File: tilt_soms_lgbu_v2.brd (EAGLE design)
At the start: 36 x 130 mm, 37 parts

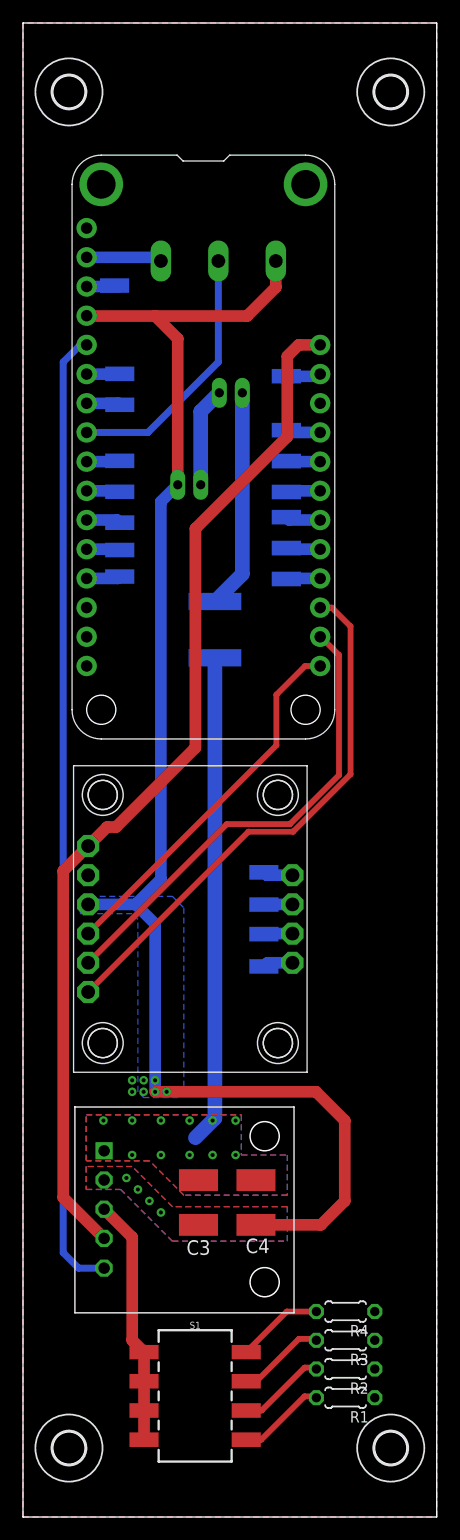
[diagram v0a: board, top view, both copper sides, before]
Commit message: Added a v2 for the tilt_soms_lgbu board (tilt_soms_lgbu_v2)
Primary changes:
Placed all components on top layer including the con-wago connectors.
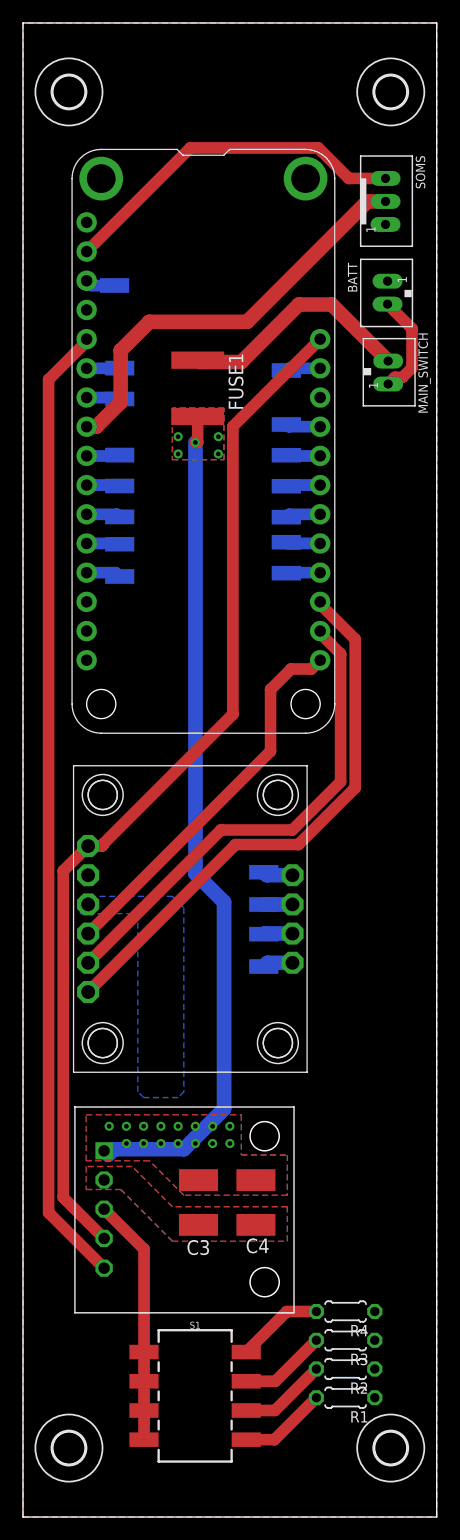
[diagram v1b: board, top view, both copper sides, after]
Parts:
- SOMS: value (none) -> JST-PH_3-PIN_HEADER; device con-wago-500:W237-103 -> SRG:JST_B3B-PH_HEADER
- moved BATT 24.0 mm to (31.8, 106.5), flipped to the top, turned to 90 degrees
- moved FUSE1 21.1 mm to (15.2, 98.2), flipped to the top
- moved SOMS 15.9 mm to (31.5, 114.5), flipped to the top, turned to 270 degrees
- moved MAIN_SWITCH 13.7 mm to (31.7, 99.7), flipped to the top, turned to 270 degrees
- moved MS1 0.50 mm to (4.27, 119.0)
- moved PAD20 0.50 mm to (8.42, 100.0)
- moved PAD21 0.50 mm to (8.42, 97.3)
- moved PAD23 0.50 mm to (8.42, 92.4)
- moved PAD24 0.50 mm to (8.42, 89.7)
- moved PAD25 0.50 mm to (8.42, 87.0)
- moved PAD27 0.50 mm to (8.42, 84.6)
- moved PAD29 0.50 mm to (22.9, 99.8)
- moved PAD30 0.50 mm to (22.9, 95.1)
- moved PAD31 0.50 mm to (22.9, 92.4)
- moved PAD32 0.50 mm to (22.9, 89.7)
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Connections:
- net FEATHER_3.3V: now also SOMS.P3; no longer SOMS.1
- net GND: now also SOMS.P1; no longer SOMS.3
- net GPIOA3: now also SOMS.P2; no longer SOMS.2
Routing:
- net GND: track 127.6 -> 0.00 mm, vias 11 -> 0
- net VOLTAGE_SUPPLY: track 42.5 -> 73.7 mm, vias 11 -> 20
- net FEATHER_3.3V: track 6.59 -> 30.8 mm
- net GPIOA3: track 22.8 -> 36.8 mm
- net N$4: track 19.1 -> 20.8 mm
- net GPIO5: track 46.9 -> 48.0 mm
- net RPI_SCL: track 41.3 -> 42.3 mm
- net RPI_SDA: track 32.4 -> 33.2 mm
- net AREF: track 3.28 -> 2.60 mm

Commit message: Reversed board. Snap to mills grid.
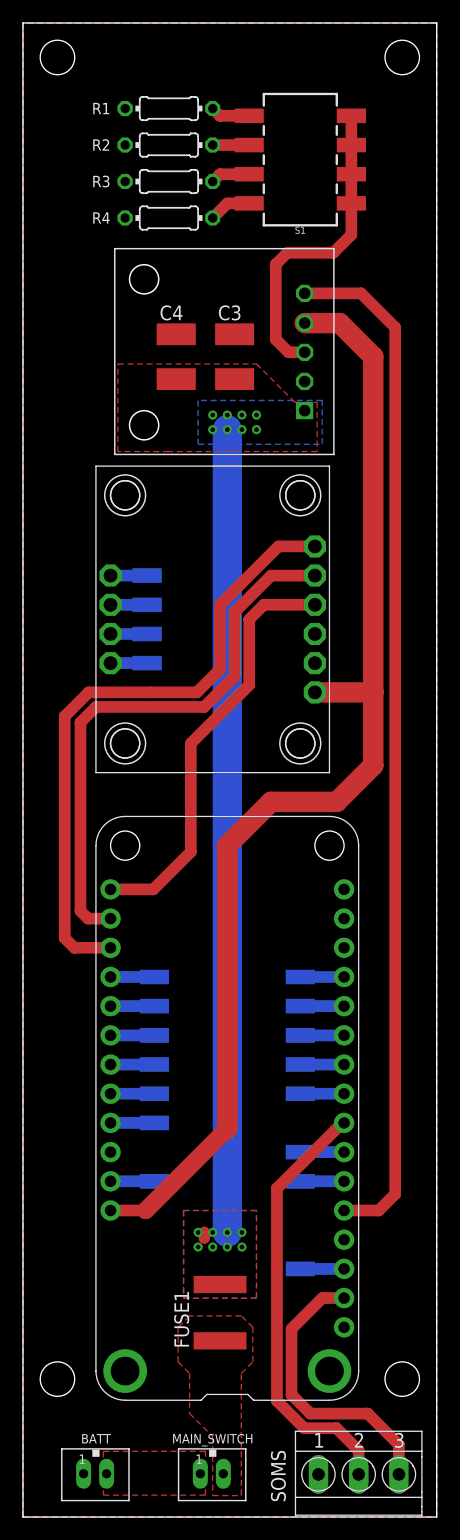
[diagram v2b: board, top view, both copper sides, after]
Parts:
- removed H5, H6, H7, H8: MOUNT-HOLE2.8, holes:2,8
- R1, R2, R3, R4: device rcl:0204/5 -> rcl:0204/7
- SOMS: value JST-PH_3-PIN_HEADER -> TERMINAL-BLOCK-3.5MM-3-PIN-LONG-PAD; device SRG:JST_B3B-PH_HEADER -> Rembrandt Electronics - Terminal Block 3-5mm v1-0:TERMINAL-BLOCK-3-PIN-3.5MM-LONG-PAD
- moved R1 113.2 mm to (12.7, 122.6), turned to 0 degrees
- moved MS1 111.7 mm to (29.2, 10.2), turned to 90 degrees
- moved SOMS 110.7 mm to (29.2, 3.81), turned to 0 degrees
- moved S1 108.0 mm to (24.1, 118.1), turned to 90 degrees
- moved R2 107.6 mm to (12.7, 119.4), turned to 0 degrees
- moved BATT 105.8 mm to (6.35, 3.81), turned to 180 degrees
- moved R3 102.0 mm to (12.7, 116.2), turned to 0 degrees
- moved MAIN_SWITCH 97.1 mm to (16.5, 3.81), turned to 180 degrees
- moved R4 96.4 mm to (12.7, 113.0), turned to 0 degrees
- moved PAD13 87.1 mm to (24.1, 21.6), turned to 270 degrees
- moved FUSE1 80.5 mm to (17.1, 17.8), turned to 90 degrees
- moved C4 73.9 mm to (13.3, 101.0), turned to 90 degrees
- moved C3 73.7 mm to (18.4, 101.0), turned to 90 degrees
- moved PAD20 72.5 mm to (24.1, 29.2), turned to 90 degrees
- moved PAD29 71.5 mm to (11.4, 29.2), turned to 90 degrees
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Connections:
- net FEATHER_3.3V: now also SOMS.3; no longer SOMS.P3
- net GND: now also SOMS.1; no longer SOMS.P1
- net GPIOA3: now also SOMS.2; no longer SOMS.P2
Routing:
- net N$4: track 20.8 -> 0.46 mm
- net FEATHER_BAT: track 89.7 -> 101.2 mm
- net N$3: track 9.07 -> 0.00 mm
- net GPIO5: track 48.0 -> 54.8 mm
- net DELAY: track 21.5 -> 27.5 mm
- net RPI_SCL: track 42.3 -> 48.3 mm
- net FEATHER_3.3V: track 30.8 -> 25.1 mm
- net DONE_PIN: track 84.2 -> 89.5 mm
- net N$10: track 7.60 -> 3.17 mm
- net N$9: track 7.62 -> 3.44 mm
- net N$11: track 7.58 -> 3.44 mm
- net N$12: track 7.57 -> 3.70 mm
- net RPI_SDA: track 33.2 -> 36.9 mm
- net VOLTAGE_SUPPLY: track 73.7 -> 70.3 mm, vias 20 -> 16
- net AREF: track 2.60 -> 3.81 mm
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- added copper zone on layer 1, net N$3
- added copper zone on layer 1, net N$4

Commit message: no dip switch
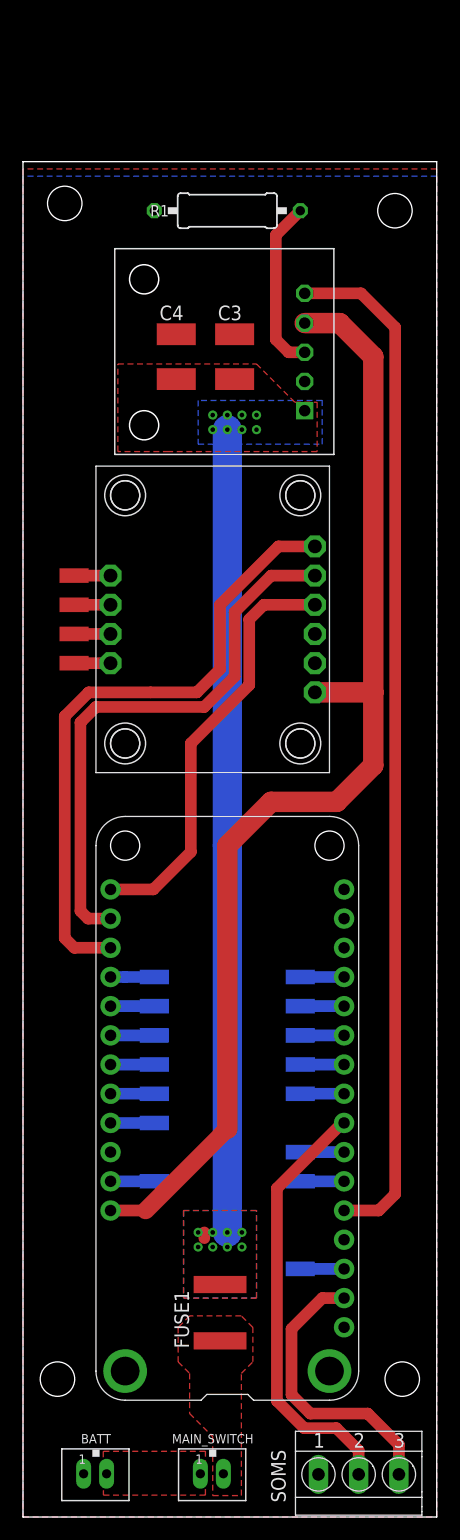
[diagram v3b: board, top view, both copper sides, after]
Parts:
- removed R2, R3, R4: (no value), rcl:0204/7
- removed S1: DIP-04SMD, SparkFun-Switches:DIPSWITCH-04-SMD
- R1: device rcl:0204/7 -> rcl:0309/12
- moved R1 10.2 mm to (17.8, 113.7)
- moved PAD37 6.35 mm to (4.45, 79.4), flipped to the top
- moved PAD38 6.35 mm to (4.45, 81.9), flipped to the top
- moved PAD39 6.35 mm to (4.45, 74.3), flipped to the top
- moved PAD40 6.35 mm to (4.45, 76.8), flipped to the top
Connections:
- removed net N$10: R2.2, S1.3
- removed net N$11: R3.2, S1.2
- removed net N$12: R4.2, S1.1
- removed net N$9: R1.2, S1.4
- net DELAY: now also R1.2; no longer S1.5, S1.6, S1.7, S1.8
- net GND: no longer R2.1, R3.1, R4.1
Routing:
- net DELAY: track 27.5 -> 15.1 mm
- net N$12: track 3.70 -> 0.00 mm
- net N$9: track 3.44 -> 0.00 mm
- net N$11: track 3.44 -> 0.00 mm
- net N$10: track 3.17 -> 0.00 mm
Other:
- board size 36 x 130 mm -> 36 x 117.9 mm
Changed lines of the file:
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@@
 <board>
 <plain>
-<wire x1="36" y1="130" x2="0" y2="130" width="0" layer="20"/>
-<wire x1="0" y1="130" x2="0" y2="0" width="0" layer="20"/>
+<wire x1="36" y1="117.935" x2="0" y2="117.935" width="0" layer="20"/>
+<wire x1="0" y1="117.935" x2="0" y2="0" width="0" layer="20"/>
 <wire x1="0" y1="0" x2="36" y2="0" width="0" layer="20"/>
-<wire x1="36" y1="0" x2="36" y2="130" width="0" layer="20"/>
+<wire x1="36" y1="0" x2="36" y2="117.935" width="0" layer="20"/>
 <dimension x1="0" y1="0" x2="0" y2="130" x3="-17.5" y3="65" textsize="1.778" layer="49"/>
 <dimension x1="0" y1="130" x2="36" y2="130" x3="18" y3="144" textsize="1.778" layer="49"/>
 <hole x="33" y="12" drill="3"/>
 <hole x="3" y="12" drill="3"/>
-<hole x="33" y="127" drill="3"/>
-<hole x="3" y="127" drill="3"/>
+<hole x="32.365" y="113.665" drill="3"/>
+<hole x="3.635" y="114.3" drill="3"/>
 </plain>
 <attributes>
@@
 <element name="PAD34" library="wirepad" package="SMD1,27-2,54" value="WIREPADSMD1,27-254" x="11.43" y="44.45" smashed="yes" rot="MR90"/>
 <element name="PAD35" library="wirepad" package="SMD1,27-2,54" value="WIREPADSMD1,27-254" x="11.43" y="46.99" smashed="yes" rot="MR90"/>
-<element name="PAD37" library="wirepad" package="SMD1,27-2,54" value="WIREPADSMD1,27-254" x="10.795" y="79.375" smashed="yes" rot="MR270"/>
-<element name="PAD38" library="wirepad" package="SMD1,27-2,54" value="WIREPADSMD1,27-254" x="10.795" y="81.915" smashed="yes" rot="MR270"/>
-<element name="PAD39" library="wirepad" package="SMD1,27-2,54" value="WIREPADSMD1,27-254" x="10.795" y="74.295" smashed="yes" rot="MR270"/>
-<element name="PAD40" library="wirepad" package="SMD1,27-2,54" value="WIREPADSMD1,27-254" x="10.795" y="76.835" smashed="yes" rot="MR270"/>
-<element name="R1" library="rcl" package="0204/7" value="" x="12.7" y="122.555" smashed="yes">
-<attribute name="NAME" x="7.62" y="122.555" size="0.9906" layer="25" ratio="10" align="center-right"/>
-<attribute name="VALUE" x="11.0744" y="122.0724" size="0.9906" layer="27" ratio="10"/>
-</element>
-<element name="R2" library="rcl" package="0204/7" value="" x="12.7" y="119.38" smashed="yes">
-<attribute name="NAME" x="7.62" y="119.38" size="0.9906" layer="25" ratio="10" align="center-right"/>
-<attribute name="VALUE" x="11.0744" y="118.8974" size="0.9906" layer="27" ratio="10"/>
-</element>
-<element name="R3" library="rcl" package="0204/7" value="" x="12.7" y="116.205" smashed="yes">
-<attribute name="NAME" x="7.62" y="116.205" size="0.9906" layer="25" ratio="10" align="center-right"/>
-<attribute name="VALUE" x="11.0744" y="115.7224" size="0.9906" layer="27" ratio="10"/>
-</element>
-<element name="R4" library="rcl" package="0204/7" value="" x="12.7" y="113.03" smashed="yes">
-<attribute name="NAME" x="7.62" y="113.03" size="0.9906" layer="25" ratio="10" align="center-right"/>
-<attribute name="VALUE" x="11.0744" y="112.5474" size="0.9906" layer="27" ratio="10"/>
-</element>
-<element name="S1" library="SparkFun-Switches" package="DIPSWITCH-04-SMD" value="DIP-04SMD" x="24.13" y="118.11" smashed="yes" rot="R90">
-<attribute name="NAME" x="24.13" y="112.268" size="0.6096" layer="25" font="vector" ratio="20" rot="R180" align="bottom-center"/>
-<attribute name="PROD_ID" value="SWCH-12418" x="24.13" y="118.11" size="1.778" layer="27" rot="R90" display="off"/>
-<attribute name="VALUE" x="24.13" y="123.952" size="0.6096" layer="27" font="vector" ratio="20" rot="R180" align="top-center"/>
+<element name="PAD37" library="wirepad" package="SMD1,27-2,54" value="WIREPADSMD1,27-254" x="4.445" y="79.375" smashed="yes" rot="R270"/>
+<element name="PAD38" library="wirepad" package="SMD1,27-2,54" value="WIREPADSMD1,27-254" x="4.445" y="81.915" smashed="yes" rot="R270"/>
+<element name="PAD39" library="wirepad" package="SMD1,27-2,54" value="WIREPADSMD1,27-254" x="4.445" y="74.295" smashed="yes" rot="R270"/>
+<element name="PAD40" library="wirepad" package="SMD1,27-2,54" value="WIREPADSMD1,27-254" x="4.445" y="76.835" smashed="yes" rot="R270"/>
+<element name="R1" library="rcl" package="0309/12" value="" x="17.78" y="113.665" smashed="yes">
+<attribute name="NAME" x="12.7" y="113.665" size="0.9906" layer="25" ratio="10" align="center-right"/>
+<attribute name="VALUE" x="16.1544" y="113.1824" size="0.9906" layer="27" ratio="10"/>
 </element>
 <element name="U$3" library="edc_modules" package="TPL5110_BREAKOUT" value="TPL5110_BREAKOUT" x="26.67" y="93.98" smashed="yes" rot="R90"/>
@@
 <contactref element="U$3" pad="GND"/>
 <contactref element="R1" pad="1"/>
-<contactref element="R2" pad="1"/>
-<contactref element="R3" pad="1"/>
-<contactref element="R4" pad="1"/>
 <contactref element="U$4" pad="GND"/>
 <contactref element="C4" pad="2"/>
@@
 <contactref element="BATT" pad="P1"/>
 <polygon width="0.254" layer="16" isolate="0.4064" rank="6">
-<vertex x="36" y="130"/>
-<vertex x="0" y="130"/>
+<vertex x="36" y="116.665"/>
+<vertex x="0" y="116.665"/>
 <vertex x="0" y="0"/>
 <vertex x="36" y="0"/>
 </polygon>
 <polygon width="0.254" layer="1" isolate="0.4064" rank="6">
-<vertex x="36" y="130"/>
-<vertex x="0" y="130"/>
+<vertex x="36" y="117.3"/>
+<vertex x="0" y="117.3"/>
 <vertex x="0" y="0"/>
 <vertex x="36" y="0"/>
@@
 <signal name="DELAY">
 <contactref element="U$3" pad="DELAY"/>
-<contactref element="S1" pad="5"/>
-<contactref element="S1" pad="6"/>
-<contactref element="S1" pad="7"/>
-<contactref element="S1" pad="8"/>
-<wire x1="28.575" y1="114.3" x2="28.575" y2="116.84" width="1.016" layer="1"/>
-<wire x1="28.575" y1="116.84" x2="28.575" y2="119.38" width="1.016" layer="1"/>
-<wire x1="28.575" y1="119.38" x2="28.575" y2="121.92" width="1.016" layer="1"/>
 <wire x1="23.114" y1="101.346" x2="22" y2="102.46" width="1.016" layer="1"/>
-<wire x1="22" y1="102.46" x2="22" y2="109" width="1.016" layer="1"/>
-<wire x1="22" y1="109" x2="23" y2="110" width="1.016" layer="1"/>
-<wire x1="23" y1="110" x2="27" y2="110" width="1.016" layer="1"/>
-<wire x1="28.575" y1="111.575" x2="28.575" y2="114.3" width="1.016" layer="1"/>
-<wire x1="27" y1="110" x2="28.575" y2="111.575" width="1.016" layer="1"/>
 <wire x1="24.511" y1="101.346" x2="23.114" y2="101.346" width="1.016" layer="1"/>
-</signal>
-<signal name="N$9">
-<contactref element="S1" pad="4"/>
 <contactref element="R1" pad="2"/>
-<wire x1="19.685" y1="121.92" x2="17.145" y2="121.92" width="1.016" layer="1"/>
-<wire x1="17.145" y1="121.92" x2="16.51" y2="122.555" width="1.016" layer="1"/>
-</signal>
-<signal name="N$10">
-<contactref element="S1" pad="3"/>
-<contactref element="R2" pad="2"/>
-<wire x1="19.685" y1="119.38" x2="16.51" y2="119.38" width="1.016" layer="1"/>
-</signal>
-<signal name="N$11">
-<contactref element="S1" pad="2"/>
-<contactref element="R3" pad="2"/>
-<wire x1="19.685" y1="116.84" x2="17.145" y2="116.84" width="1.016" layer="1"/>
-<wire x1="16.51" y1="116.205" x2="17.145" y2="116.84" width="1.016" layer="1"/>
-</signal>
-<signal name="N$12">
-<contactref element="S1" pad="1"/>
-<contactref element="R4" pad="2"/>
-<wire x1="19.685" y1="114.3" x2="17.78" y2="114.3" width="1.016" layer="1"/>
-<wire x1="17.78" y1="114.3" x2="16.51" y2="113.03" width="1.016" layer="1"/>
+<wire x1="22" y1="111.535" x2="24.13" y2="113.665" width="1.016" layer="1"/>
+<wire x1="22" y1="102.46" x2="22" y2="111.535" width="1.016" layer="1"/>
 </signal>
 <signal name="DONE_PIN">
@@
 <contactref element="U$4" pad="INT"/>
 <contactref element="PAD37" pad="1"/>
-<wire x1="10.795" y1="79.375" x2="7.62" y2="79.375" width="1.016" layer="16"/>
+<wire x1="7.62" y1="79.375" x2="4.445" y2="79.375" width="1.016" layer="1"/>
 </signal>
 <signal name="N$5">
 <contactref element="U$4" pad="ADR"/>
 <contactref element="PAD38" pad="1"/>
-<wire x1="10.795" y1="81.915" x2="7.62" y2="81.915" width="1.016" layer="16"/>
+<wire x1="7.62" y1="81.915" x2="4.445" y2="81.915" width="1.016" layer="1"/>
 </signal>
 <signal name="N$6">
 <contactref element="U$4" pad="PS0"/>
 <contactref element="PAD39" pad="1"/>
-<wire x1="10.795" y1="74.295" x2="7.62" y2="74.295" width="1.016" layer="16"/>
+<wire x1="7.62" y1="74.295" x2="4.445" y2="74.295" width="1.016" layer="1"/>
 </signal>
 <signal name="N$7">
 <contactref element="U$4" pad="PS1"/>
 <contactref element="PAD40" pad="1"/>
-<wire x1="10.795" y1="76.835" x2="7.62" y2="76.835" width="1.016" layer="16"/>
+<wire x1="7.62" y1="76.835" x2="4.445" y2="76.835" width="1.016" layer="1"/>
 </signal>
 <signal name="FEATHER_BAT">
